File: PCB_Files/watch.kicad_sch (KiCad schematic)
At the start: 117 parts, among them J1 Conn_01x02_Pin, J2 Conn_01x14_MountingPin, J3 Conn_01x02_Pin, P1 USB_C_Plug_USB2.0, Q1 BC847, Q2 BC847, Q4 BSS138, Q5 BSS138, Q8 BC847, SW1 SW_Push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

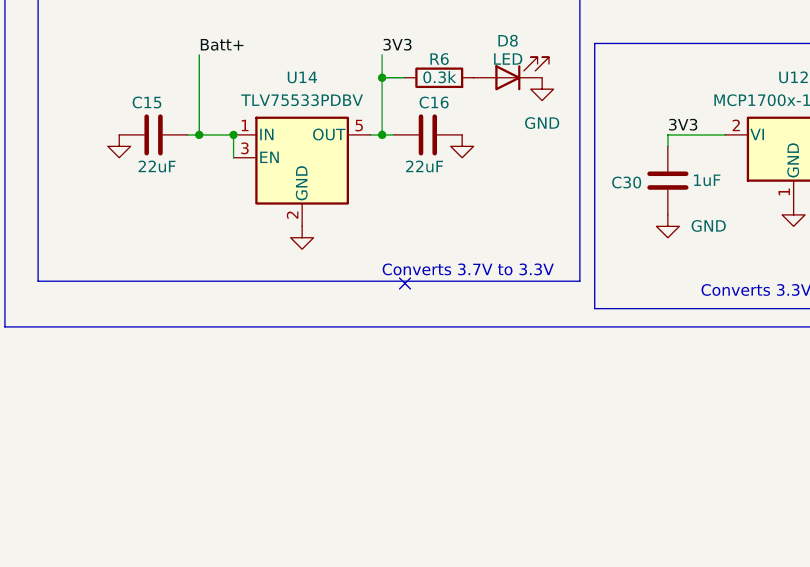
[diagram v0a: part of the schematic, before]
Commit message: Did routing of ESP, USB, USB-to-TTL, RAM, Flash, Osscilator & PMIC
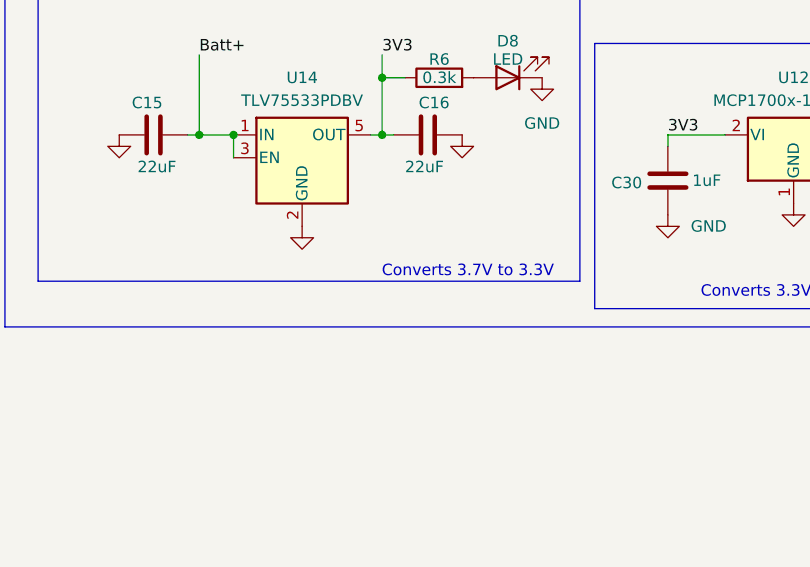
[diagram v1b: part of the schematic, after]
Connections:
- no-connect marks 34 -> 33
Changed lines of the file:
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@@
 	)
 	(no_connect
-		(at 436.88 105.41)
-	)
-	(no_connect
 		(at 143.51 300.99)
 	)
@@
 		(on_board yes)
 		(dnp no)
-		(fields_autoplaced yes)
 		(property "Reference" "C1"
 			(at 48.26 77.4699 0)

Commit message: Restarted routing
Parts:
- added JP2: SolderJumper_2_Open, Resistor_SMD:R_0402_1005Metric, symbol Jumper:SolderJumper_2_Open
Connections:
- net 3V3: now also JP2.2 (B); no longer U4.8 (VCC)
- net BL_PWM: now also R37.2
- net CE: no longer U2.25 (IO16)
- net GND: now also Q8.2 (E)
- net LEDK: now also R36.2
- net at U2.3 (VDDA3P3), U2.4 (VDDA3P3): no longer C8.1, L1.1
- net at Q8.1 (B): now also R37.1; no longer R37.2
- new net: JP2.1 (A), U4.8 (VCC)
- new net: C8.1, L1.1
- no-connect marks 33 -> 34
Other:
- moved on the sheet: C10, C12, C8, C9, L1, Q8, R36, R37

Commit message: Completed layout
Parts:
- removed R26, R27: 33, Resistor_SMD:R_0603_1608Metric, symbol Device:R
- added R13, R7: 10k, Resistor_SMD:R_0603_1608Metric, symbol Device:R
- D9: footprint footprints:SOD-123FL -> Diode_SMD:D_SOD-123
- FB1: value FerriteBead -> 2.66
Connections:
- net SCL_i2c: now also R7.1
- net SDA: now also R13.1
- net at U2.3 (VDDA3P3), U2.4 (VDDA3P3): now also C8.1, L1.1
- net at U11.16 (SDA): now also R13.2
- net at U11.17 (SCL): now also R7.2
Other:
- moved on the sheet: C10, C12, C8, C9, L1

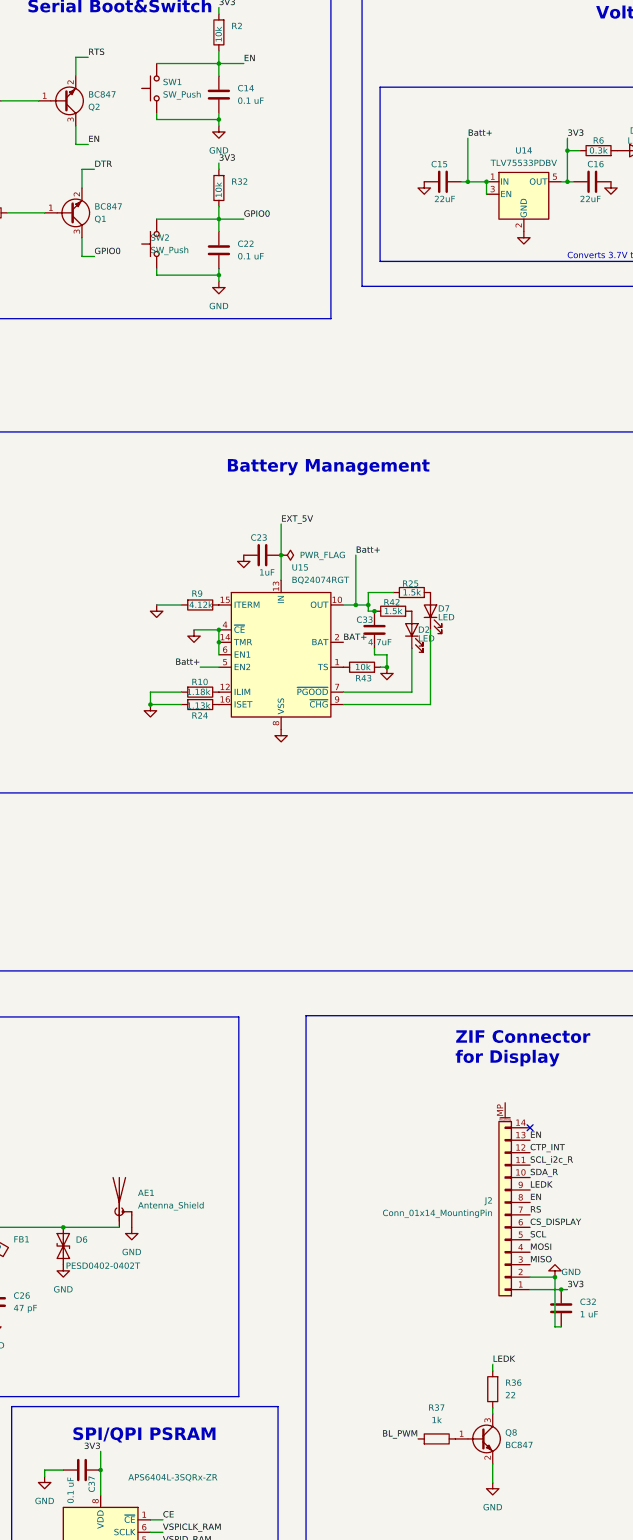
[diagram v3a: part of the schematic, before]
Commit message: Did impedance matching of antennas
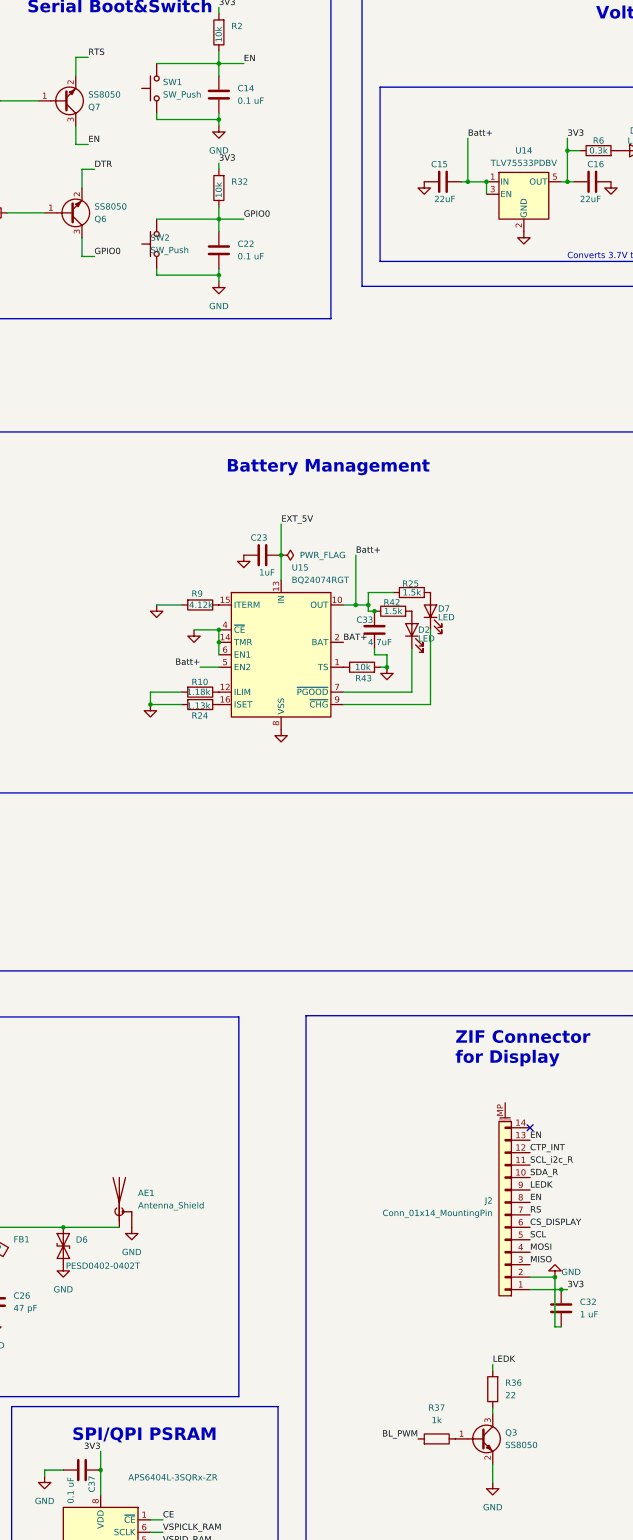
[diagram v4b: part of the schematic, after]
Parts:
- removed Q1, Q2, Q8: BC847, Package_TO_SOT_SMD:SOT-23, symbol Transistor_BJT:BC847
- added Q3, Q6, Q7: SS8050, Package_TO_SOT_SMD:SOT-23, symbol Transistor_BJT:SS8050
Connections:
- net DTR: now also Q6.2 (E)
- net EN: now also Q7.3 (C)
- net GND: now also Q3.2 (E)
- net GPIO0: now also Q6.3 (C)
- net RTS: now also Q7.2 (E)
- net at R37.1: now also Q3.1 (B)
- net at R36.1: now also Q3.3 (C)
- net at R12.1: now also Q7.1 (B)
- net at R11.1: now also Q6.1 (B)

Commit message: Improving Antenna routing
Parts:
- removed R40, R41: 10k, Resistor_SMD:R_0603_1608Metric, symbol Device:R
- removed TP7, TP8: TestPoint, TestPoint:TestPoint_Pad_D1.0mm, symbol Connector:TestPoint
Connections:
- net BTN1: no longer names the net of U2.5 (SENSOR_VP)
- net BTN2: no longer names the net of U2.8 (SENSOR_VN)
- no-connect marks 34 -> 36

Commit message: Fixed some routing
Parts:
- C26: footprint Capacitor_SMD:C_0603_1608Metric -> Capacitor_SMD:C_0402_1005Metric
- FB1: footprint Inductor_SMD:L_0603_1608Metric -> Inductor_SMD:L_0402_1005Metric
- R28: footprint Resistor_SMD:R_0603_1608Metric -> Resistor_SMD:R_0402_1005Metric
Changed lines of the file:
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@@
 			)
 		)
-		(property "Footprint" "Inductor_SMD:L_0603_1608Metric"
+		(property "Footprint" "Inductor_SMD:L_0402_1005Metric"
 			(at 315.722 306.07 90)
 			(effects
@@
 			)
 		)
-		(property "Footprint" "Resistor_SMD:R_0603_1608Metric"
+		(property "Footprint" "Resistor_SMD:R_0402_1005Metric"
 			(at 292.608 279.4 90)
 			(effects
@@
 			)
 		)
-		(property "Footprint" "Capacitor_SMD:C_0603_1608Metric"
+		(property "Footprint" "Capacitor_SMD:C_0402_1005Metric"
 			(at 318.4652 321.31 0)
 			(effects
